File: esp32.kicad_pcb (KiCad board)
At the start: 2 copper layers, 25.4 x 41.4 mm, 20 parts, among them IC1 ESP32-WROVER-E_M213EH6464PH3Q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, J1 Micro_SD_Card_Det, J2 Conn_01x10_Male, J3 Conn_01x10_Male, U1 MCP2518FDT-H_SL, U2 SN65HVD231, Y1 XRCGB40M000F4M02R0

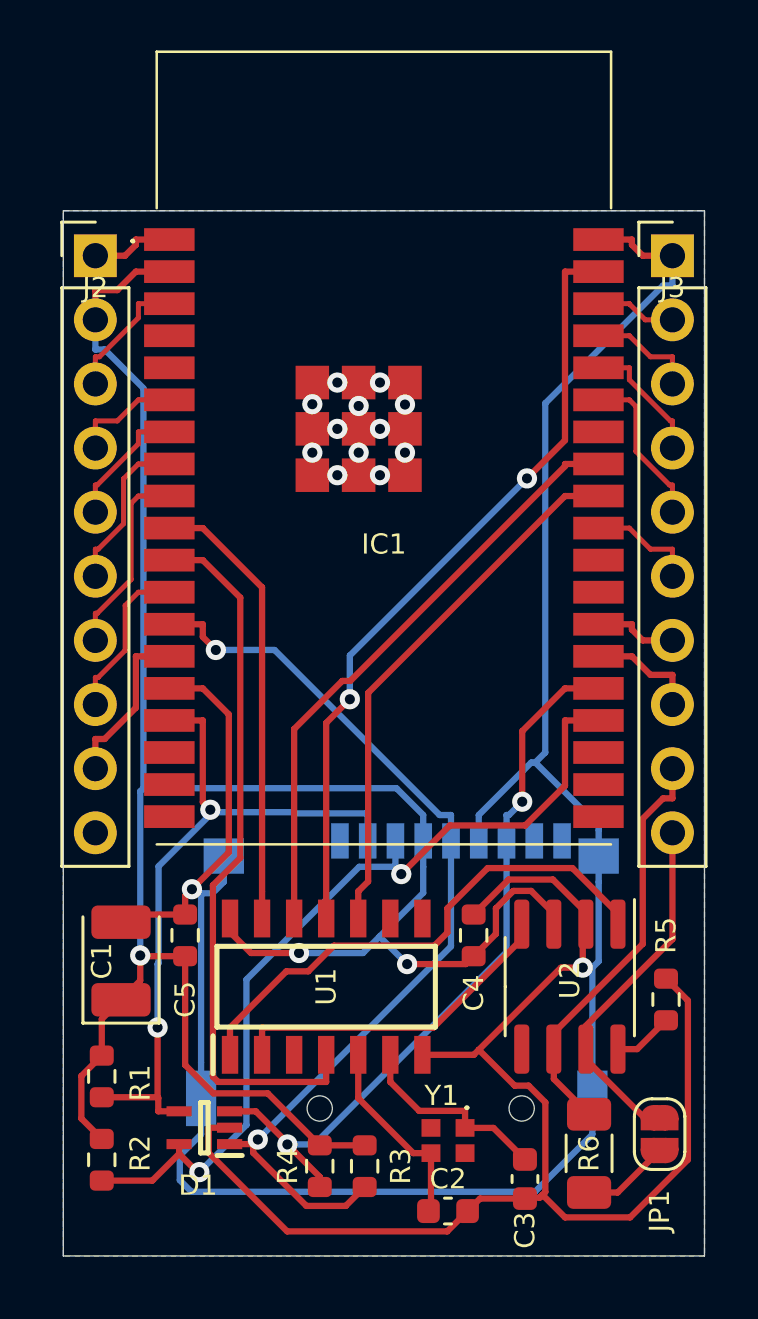
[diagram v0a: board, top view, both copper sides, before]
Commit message: EN Pullup, DTR + RTS
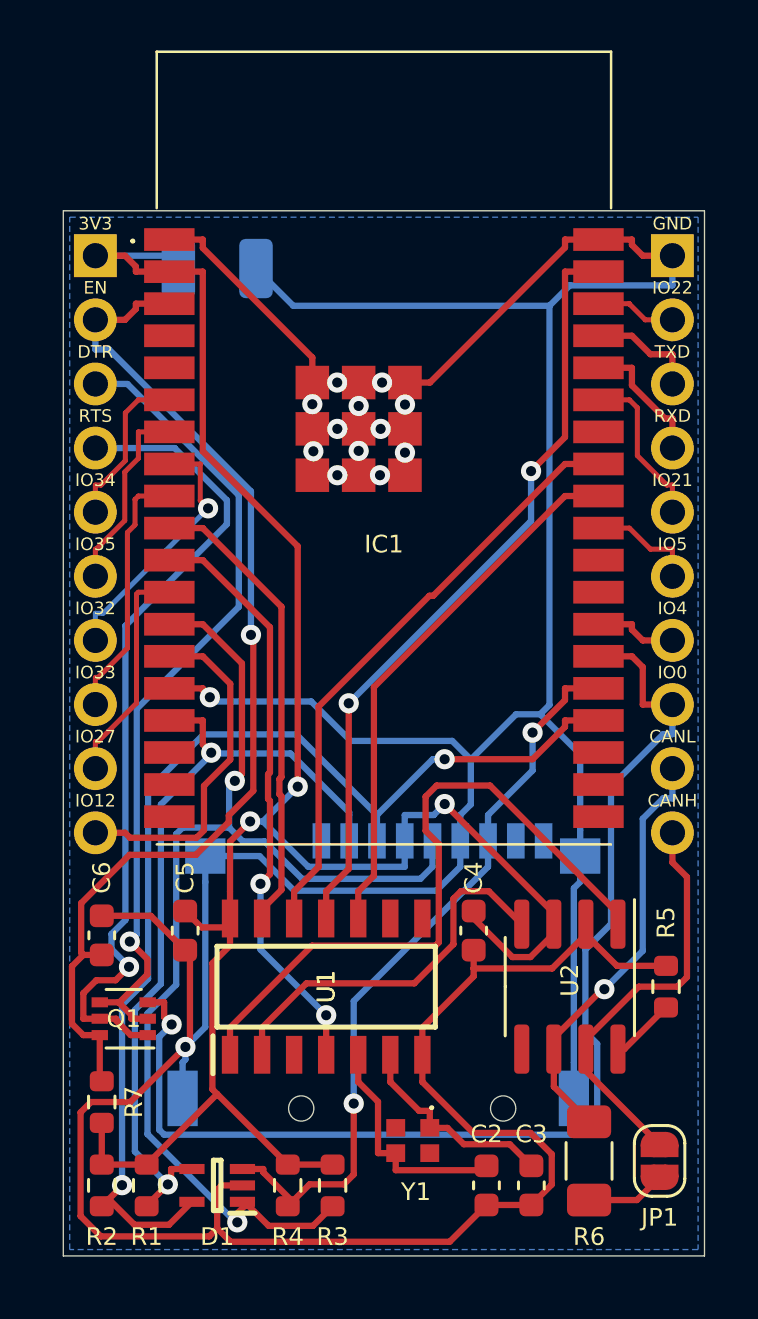
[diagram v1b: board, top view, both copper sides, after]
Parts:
- added C6: 100nF, Capacitor_SMD:C_0603_1608Metric, F.Cu at (86.6, 93.0)
- added Q1: UMH3N, Package_TO_SOT_SMD:SOT-363_SC-70-6, F.Cu at (87.5, 96.3)
- added R7: 10k, Resistor_SMD:R_0603_1608Metric, F.Cu at (86.6, 99.6)
- C1, J2, J3: moved to B.Cu
- C4, C5: footprint Resistor_SMD:R_0603_1608Metric -> Capacitor_SMD:C_0603_1608Metric
- R1, R2, R3, R4: value R -> 10k
- moved C1 27.7 mm to (91.2, 66.5), turned to 0 degrees
- moved R1 4.67 mm to (88.4, 102.9)
- moved D1 2.34 mm to (91.2, 102.9)
- moved C2 1.83 mm to (101.9, 102.9), turned to 90 degrees
- moved R3 1.48 mm to (95.8, 102.9)
- moved R4 1.48 mm to (94.0, 102.9)
- moved Y1 1.40 mm to (98.9, 101.1)
- moved JP1 1.06 mm to (108.7, 101.9)
- moved R2 1.02 mm to (86.6, 102.9)
- moved J1 0.73 mm to (97.6, 99.8)
- moved R5 0.51 mm to (109.0, 95.0)
- moved C3 0.36 mm to (103.6, 102.9)
- moved R6 0.30 mm to (105.9, 101.9)
- moved C4 0.19 mm to (101.3, 92.8), turned to 270 degrees
- moved C5 0.19 mm to (89.9, 92.8), turned to 270 degrees
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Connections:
- net Net-(IC1-Pad25) renamed IO0
- net Net-(IC1-Pad34) renamed RXD
- net Net-(IC1-Pad35) renamed TXD
- IC1 pad 3: Net-(IC1-Pad3) -> EN
- J2 pad 1: GND -> +3V3
- J2 pad 10: Net-(J2-Pad10) -> Net-(IC1-Pad14)
- J2 pad 2: +3V3 -> EN
- J2 pad 3: Net-(IC1-Pad3) -> DTR
- J2 pad 4: Net-(IC1-Pad6) -> RTS
- J2 pad 5: Net-(IC1-Pad7) -> Net-(IC1-Pad6)
- J2 pad 6: Net-(IC1-Pad8) -> Net-(IC1-Pad7)
- J2 pad 7: Net-(IC1-Pad9) -> Net-(IC1-Pad8)
- J2 pad 8: Net-(IC1-Pad12) -> Net-(IC1-Pad9)
- J2 pad 9: Net-(IC1-Pad14) -> Net-(IC1-Pad12)
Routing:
- net EN: track 0.00 -> 42.6 mm, vias 0 -> 1
- net IO0: track 4.41 -> 46.8 mm, vias 0 -> 1
- net RTS: track 0.00 -> 32.8 mm, vias 0 -> 1
- net DTR: track 0.00 -> 32.4 mm, vias 0 -> 1
- net GND: track 172.4 -> 198.3 mm
- net SD_CMD: track 34.4 -> 44.1 mm
- net SD_CLK: track 37.7 -> 45.0 mm
- net +3V3: track 87.8 -> 80.8 mm
- net Net-(IC1-Pad14): track 6.66 -> 13.6 mm
- net Net-(U1-Pad1): track 20.8 -> 27.1 mm
- net Net-(IC1-Pad3): track 5.21 -> 0.00 mm
- net MCP_INT: track 28.5 -> 23.3 mm, vias 0 -> 2
- net Net-(IC1-Pad8): track 6.45 -> 10.4 mm, vias 0 -> 1
- net SD_DAT3: track 28.1 -> 31.9 mm
- net Net-(IC1-Pad9): track 7.70 -> 10.3 mm
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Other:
- board text added: "3V3"
- board text added: "CANH"
- board text added: "CANL"
- board text added: "DTR"
- board text added: "EN"
- board text added: "GND"
- board text added: "IO0"
- board text added: "IO12"
- board text added: "IO21"
- board text added: "IO22"
- board text added: "IO27"
- board text added: "IO32"
- board text added: "IO33"
- board text added: "IO34"
- board text added: "IO35"
- board text added: "IO4"
- board text added: "IO5"
- board text added: "RTS"
- board text added: "RXD"
- board text added: "TXD"

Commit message: Alle ESP Pins
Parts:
- removed Q1: UMH3N, Package_TO_SOT_SMD:SOT-363_SC-70-6
- J2: value Conn_01x10_Male -> Conn_01x14_Male; footprint Connector_PinHeader_2.54mm:PinHeader_1x10_P2.54mm_Vertical -> Connector_PinHeader_2.54mm:PinHeader_1x14_P2.54mm_Vertical
- J3: value Conn_01x10_Male -> Conn_01x16_Male; footprint Connector_PinHeader_2.54mm:PinHeader_1x10_P2.54mm_Vertical -> Connector_PinHeader_2.54mm:PinHeader_1x16_P2.54mm_Vertical
- moved C6 5.00 mm to (88.6, 97.5)
- moved C2 3.09 mm to (98.9, 103.9), turned to 180 degrees
- moved JP1 3.09 mm to (105.9, 100.6), turned to 180 degrees
- moved R5 2.90 mm to (107.2, 92.7)
- moved R7 2.59 mm to (89.2, 100.1), turned to 180 degrees
- moved U2 1.78 mm to (103.4, 95.0)
- moved C3 1.52 mm to (102.1, 102.9)
- moved C4 1.52 mm to (99.8, 92.8)
- moved U1 1.52 mm to (94.0, 95.0)
- moved R6 1.42 mm to (105.4, 103.2), turned to 180 degrees
- moved C5 1.27 mm to (88.6, 92.8)
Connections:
- J2 pad 10: Net-(IC1-Pad14) -> MCP_INT
- J2 pad 3: DTR -> Net-(IC1-Pad4)
- J2 pad 4: RTS -> Net-(IC1-Pad5)
- J2 pad 9: Net-(IC1-Pad12) -> MCP_CS
- J3 pad 10: CANH -> Net-(IC1-Pad26)
- J3 pad 2: Net-(IC1-Pad36) -> MCP_MOSI
- J3 pad 3: TXD -> Net-(IC1-Pad36)
- J3 pad 4: RXD -> TXD
- J3 pad 5: Net-(IC1-Pad33) -> RXD
- J3 pad 6: Net-(IC1-Pad29) -> Net-(IC1-Pad33)
- J3 pad 7: Net-(IC1-Pad26) -> MCP_MISO
- J3 pad 8: IO0 -> MCP_CLK
- J3 pad 9: CANL -> Net-(IC1-Pad29)
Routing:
- net IO0: track 46.8 -> 13.0 mm
- net RTS: track 32.8 -> 0.00 mm, vias 1 -> 0
- net DTR: track 32.4 -> 0.00 mm, vias 1 -> 0
- net GND: track 198.3 -> 172.2 mm, vias 14 -> 18
- net MCP_INT: track 23.3 -> 38.1 mm, vias 2 -> 3
- net SD_CMD: track 44.1 -> 58.2 mm, vias 2 -> 1
- net MCP_CS: track 18.5 -> 30.9 mm, vias 0 -> 2
- net SD_DAT0: track 29.8 -> 38.5 mm
- net MCP_CLK: track 21.5 -> 29.2 mm, vias 0 -> 1
- net Net-(IC1-Pad29): track 4.35 -> 11.6 mm
- net Net-(IC1-Pad26): track 3.32 -> 10.5 mm
- net CANH: track 16.4 -> 9.21 mm
- net MCP_MISO: track 23.9 -> 30.9 mm, vias 0 -> 2
- net SD_CLK: track 45.0 -> 50.4 mm
- net Net-(IC1-Pad5): track 0.00 -> 5.37 mm
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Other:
- board size 25.4 x 41.4 mm -> 25.4 x 41.8 mm
- board text added: "IO13"
- board text added: "IO14"
- board text added: "IO15"
- board text added: "IO18"
- board text added: "IO19"
- board text added: "IO2"
- board text added: "IO23"
- board text added: "IO25"
- board text added: "IO26"
- board text added: "SVN"
- board text added: "SVP"
- board text removed: "DTR"
- board text removed: "RTS"

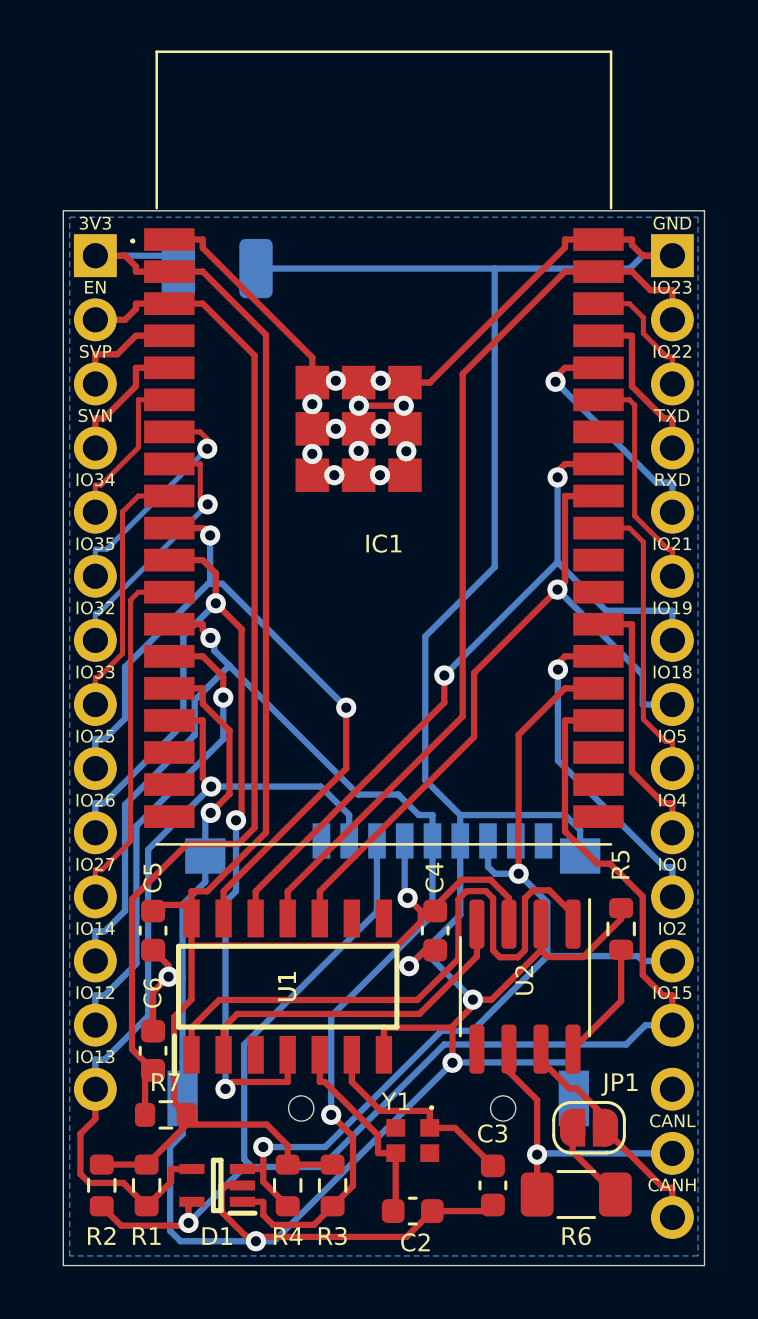
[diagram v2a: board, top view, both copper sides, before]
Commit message: ESP32 Bus extrahiert
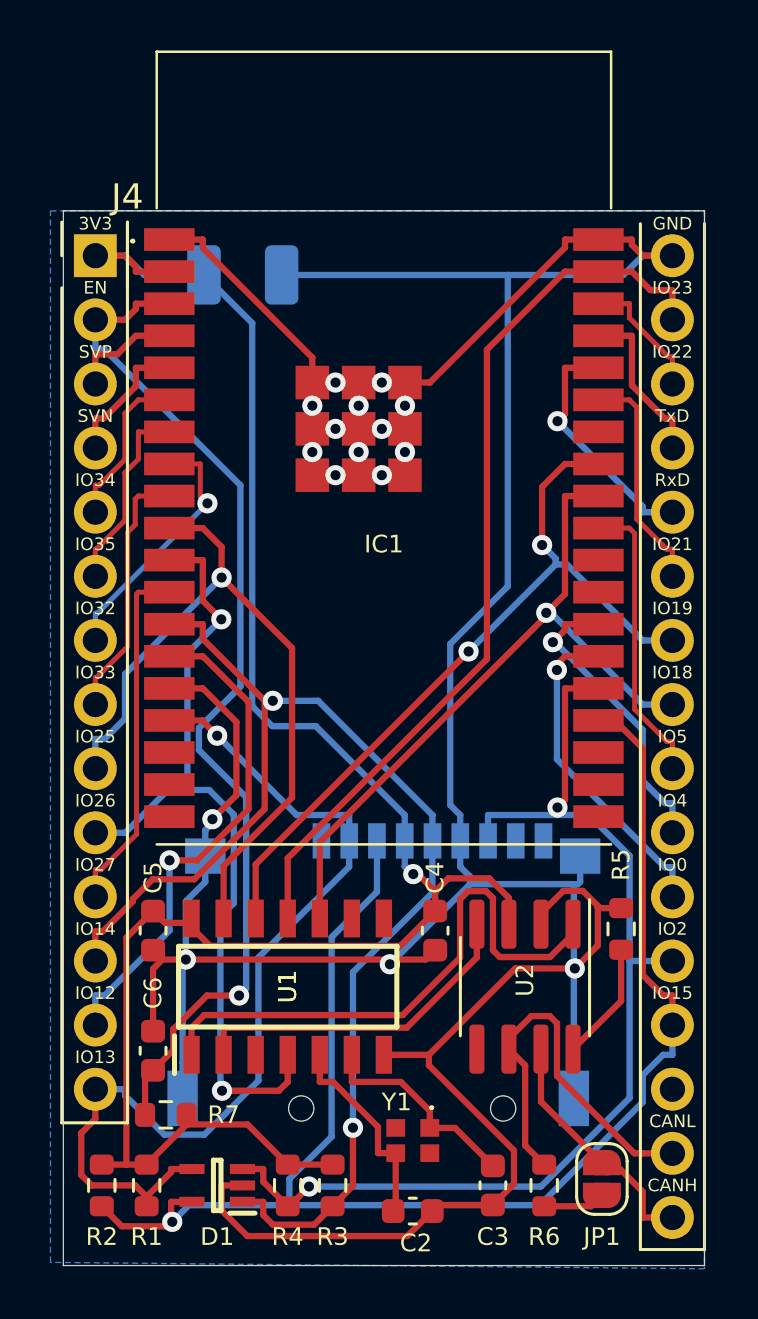
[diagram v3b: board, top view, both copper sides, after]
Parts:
- removed J2: Conn_01x14_Male, Connector_PinHeader_2.54mm:PinHeader_1x14_P2.54mm_Vertical
- removed J3: Conn_01x16_Male, Connector_PinHeader_2.54mm:PinHeader_1x16_P2.54mm_Vertical
- added J4: Bus_Connector, esp32bus:PinHeader, F.Cu at (86.4, 66.0)
- R6: footprint Resistor_SMD:R_1206_3216Metric_Pad1.30x1.75mm_HandSolder -> Resistor_SMD:R_0603_1608Metric
- moved JP1 2.09 mm to (106.4, 102.6), turned to 270 degrees
- moved R6 1.32 mm to (104.1, 102.9), turned to 90 degrees
- moved C1 1.05 mm to (92.2, 66.8)
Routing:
- net GND: track 172.2 -> 163.9 mm, vias 18 -> 16
- net MCP_INT: track 38.1 -> 32.9 mm, vias 3 -> 2
- net SD_DAT0: track 38.5 -> 43.1 mm
- net CANL: track 11.6 -> 15.9 mm, vias 1 -> 0
- net SD_DAT3: track 34.6 -> 38.2 mm
- net Net-(U1-Pad1): track 25.2 -> 22.8 mm
- net MCP_CS: track 30.9 -> 29.2 mm, vias 2 -> 1
- net Net-(IC1-Pad26): track 10.5 -> 12.0 mm, vias 0 -> 1
- net Net-(IC1-Pad7): track 9.16 -> 7.67 mm, vias 1 -> 0
- net Net-(IC1-Pad14): track 18.6 -> 20.1 mm
- net Net-(JP1-Pad2): track 3.35 -> 2.46 mm
- net SD_CMD: track 58.2 -> 58.9 mm
- net MCP_CLK: track 29.2 -> 28.6 mm
- net SD_CLK: track 50.4 -> 49.8 mm
- net CANH: track 9.21 -> 9.79 mm
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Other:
- board text removed: "3V3"
- board text removed: "CANH"
- board text removed: "CANL"
- board text removed: "EN"
- board text removed: "GND"
- board text removed: "IO0"
- board text removed: "IO12"
- board text removed: "IO13"
- board text removed: "IO14"
- board text removed: "IO15"
- board text removed: "IO18"
- board text removed: "IO19"
- board text removed: "IO2"
- board text removed: "IO21"
- board text removed: "IO22"
- board text removed: "IO23"
- board text removed: "IO25"
- board text removed: "IO26"
- board text removed: "IO27"
- board text removed: "IO32"
- board text removed: "IO33"
- board text removed: "IO34"
- board text removed: "IO35"
- board text removed: "IO4"
- board text removed: "IO5"
- board text removed: "RXD"
- board text removed: "SVN"
- board text removed: "SVP"
- board text removed: "TXD"

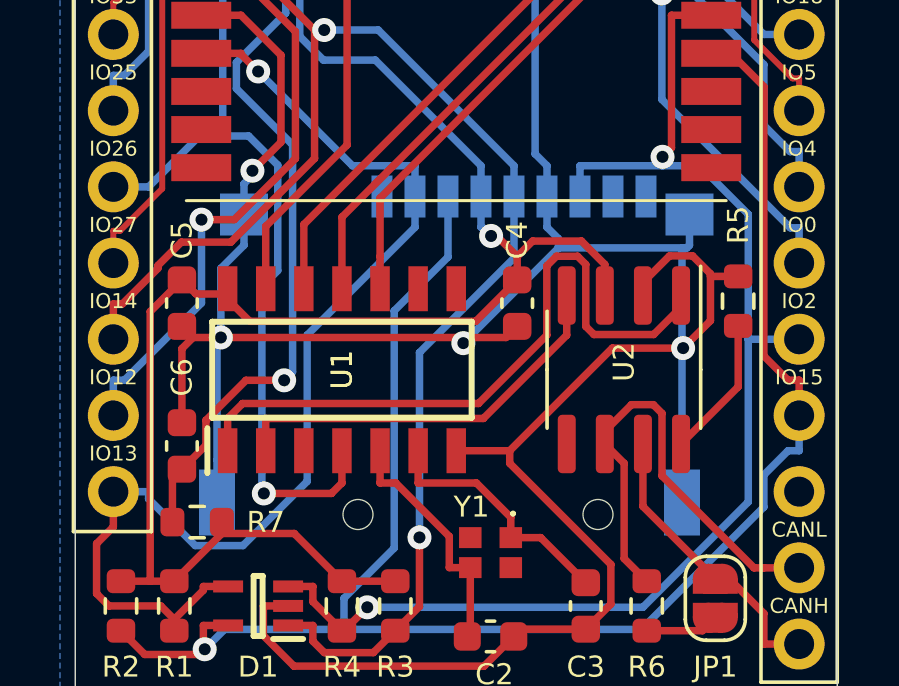
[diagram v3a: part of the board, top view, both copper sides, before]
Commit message: SD Card und MCP extrahiert
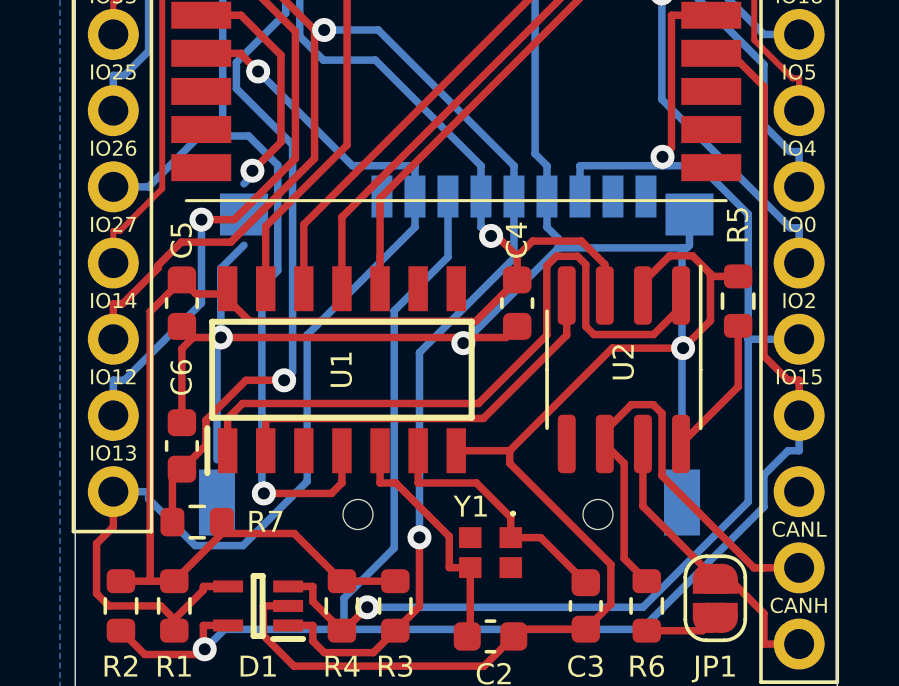
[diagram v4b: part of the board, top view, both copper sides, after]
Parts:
- D1: footprint SamacSys_Parts:SOT65P210X110-5N -> sdcard:SOT65P210X110-5N
- J1: footprint esp32:SD_CTF-11081-P -> sdcard:SD_CTF-11081-P
- U1: footprint SamacSys_Parts:SOIC127P600X175-14N -> mcp2518:SOIC127P600X175-14N
- Y1: footprint SamacSys_Parts:XRCGB40M000F4M02R0 -> mcp2518:XRCGB40M000F4M02R0
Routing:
- net GND: track 163.9 -> 159.0 mm

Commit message: Aktualisiert mit master
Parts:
- removed D1: D5V0L4B5S-7, sdcard:SOT65P210X110-5N
- added U3: SRV05-4, Package_TO_SOT_SMD:SOT-23-6, F.Cu at (91.2, 103.0)
- moved R3 9.27 mm to (86.5, 102.9)
- moved R1 5.59 mm to (94.0, 103.0)
- moved R4 1.78 mm to (95.8, 103.0)
- moved R2 1.65 mm to (88.3, 102.9)
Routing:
- net GND: track 159.0 -> 166.0 mm, vias 16 -> 14
- net SD_CLK: track 49.8 -> 44.1 mm, vias 2 -> 1
- net MCP_INT: track 32.9 -> 27.9 mm
- net +3V3: track 76.5 -> 81.4 mm, vias 1 -> 3
- net SD_CMD: track 58.9 -> 54.7 mm
- net Net-(U1-Pad1): track 22.8 -> 18.7 mm
- net Net-(IC1-Pad14): track 20.1 -> 24.0 mm
- net SD_DAT3: track 38.2 -> 34.6 mm, vias 1 -> 2
- net Net-(U1-Pad2): track 13.6 -> 16.0 mm, vias 0 -> 2
- net SD_DAT0: track 43.1 -> 45.5 mm
- net EN: track 41.3 -> 39.7 mm
- net MCP_MISO: track 30.7 -> 32.0 mm
